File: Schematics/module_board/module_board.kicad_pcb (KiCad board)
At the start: 2 copper layers, 30 x 30 mm, 35 parts, among them J1 Conn_01x01_Male, J11 Conn_01x01_Male, J12 Conn_01x01_Male, J13 Conn_01x01_Male, J14 Conn_01x01_Male, J15 Conn_01x01_Male, J16 Conn_01x01_Male, J17 Conn_01x01_Male, J2 Conn_01x01_Male, J3 Conn_01x01_Male, J4 Conn_01x01_Male, J5 Conn_01x06_Male, U1 RP2040, U2 W25Q16JVSSIQ, Y1 ABLS-12.000MHZ-B4-T

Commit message: Module updates
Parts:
- removed J11, J12, J13, J14, J15, J16, J17: Conn_01x01_Male, Connector_Pin:Pin_D1.0mm_L10.0mm
- removed REF**, hello: MountingHole_3.2mm_M3, MountingHole:MountingHole_3.2mm_M3
- added J6: Conn_01x02_Female, Connector_PinHeader_2.54mm:PinHeader_1x02_P2.54mm_Vertical, F.Cu at (172.7, 77.3)
- added J7: Conn_01x02_Female, Connector_PinHeader_2.54mm:PinHeader_1x02_P2.54mm_Vertical, F.Cu at (172.0, 99.3)
- added J8: Conn_01x02_Female, Connector_PinHeader_2.54mm:PinHeader_1x02_P2.54mm_Vertical, F.Cu at (147.6, 86.4)
- added J9: Conn_01x02_Female, Connector_PinHeader_2.54mm:PinHeader_1x02_P2.54mm_Vertical, F.Cu at (147.6, 92.1)
- J5: footprint Prototroller:Mag_Pogo_6P_P2.2mm_Male -> prototroller_footprints:Mag_Pogo_6P_P2.2mm_Male
- Y1: footprint ABLS-12:XTAL_ABLS-12.000MHZ-B4-T -> prototroller_footprints:XTAL_ABLS-12.000MHZ-B4-T
- moved JP1 10.5 mm to (151.7, 88.2)
- moved C3 4.36 mm to (167.4, 81.6)
- moved C6 4.36 mm to (169.8, 81.6)
- moved C4 4.36 mm to (168.6, 81.6)
- moved C5 4.36 mm to (166.1, 81.6)
- moved R8 3.61 mm to (162.2, 77.4)
- moved U2 3.55 mm to (156.8, 80.5)
- moved C10 3.36 mm to (163.4, 77.4)
- moved C1 3.36 mm to (162.7, 80.1)
- moved J3 3.21 mm to (169.1, 96.3)
- moved Y1 2.62 mm to (158.4, 102.1)
- moved R5 2.13 mm to (151.0, 79.5)
- moved J2 2.05 mm to (165.5, 98.0)
- moved J4 2.05 mm to (163.3, 98.0)
- moved J1 2.05 mm to (167.7, 98.0)
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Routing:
- net +3V3: track 62.9 -> 75.5 mm, vias 4 -> 5
- net +1V1: track 17.8 -> 29.0 mm, vias 0 -> 4
- net /BOOTSEL_N: track 2.68 -> 10.0 mm
- net /QSPI_SD1: track 11.7 -> 15.6 mm
- net /GPIO27_ADC1: track 23.3 -> 20.3 mm, vias 2 -> 1
- net /QSPI_SD2: track 11.3 -> 8.42 mm, vias 2 -> 0
- net Net-(C8-Pad2): track 9.48 -> 6.87 mm
- net /QSPI_SCLK: track 5.72 -> 7.62 mm
- net /XTAL_IN: track 10.8 -> 12.7 mm
- net /QSPI_NSS: track 28.3 -> 26.5 mm
- net /QSPI_SD3: track 7.35 -> 8.84 mm
- net /SPI1_SCK: track 12.1 -> 10.8 mm, vias 0 -> 1
- net /RX: track 9.78 -> 10.9 mm
- net /GPIO26_ADC0: track 22.8 -> 21.9 mm, vias 2 -> 1
- net GND: track 17.5 -> 16.6 mm, vias 16 -> 15
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
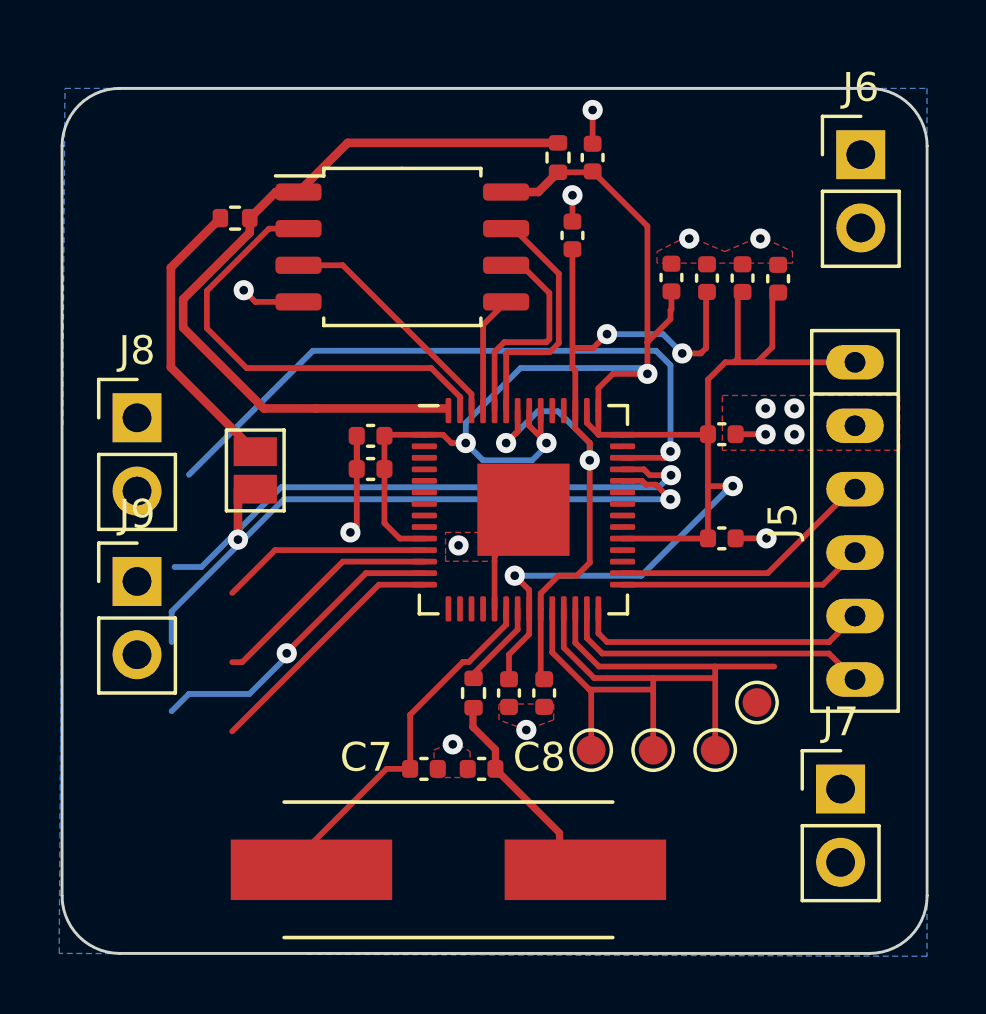
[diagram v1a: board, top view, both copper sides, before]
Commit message: Added 2.54mm pitch male headers for SPI1 pins and ADC pins
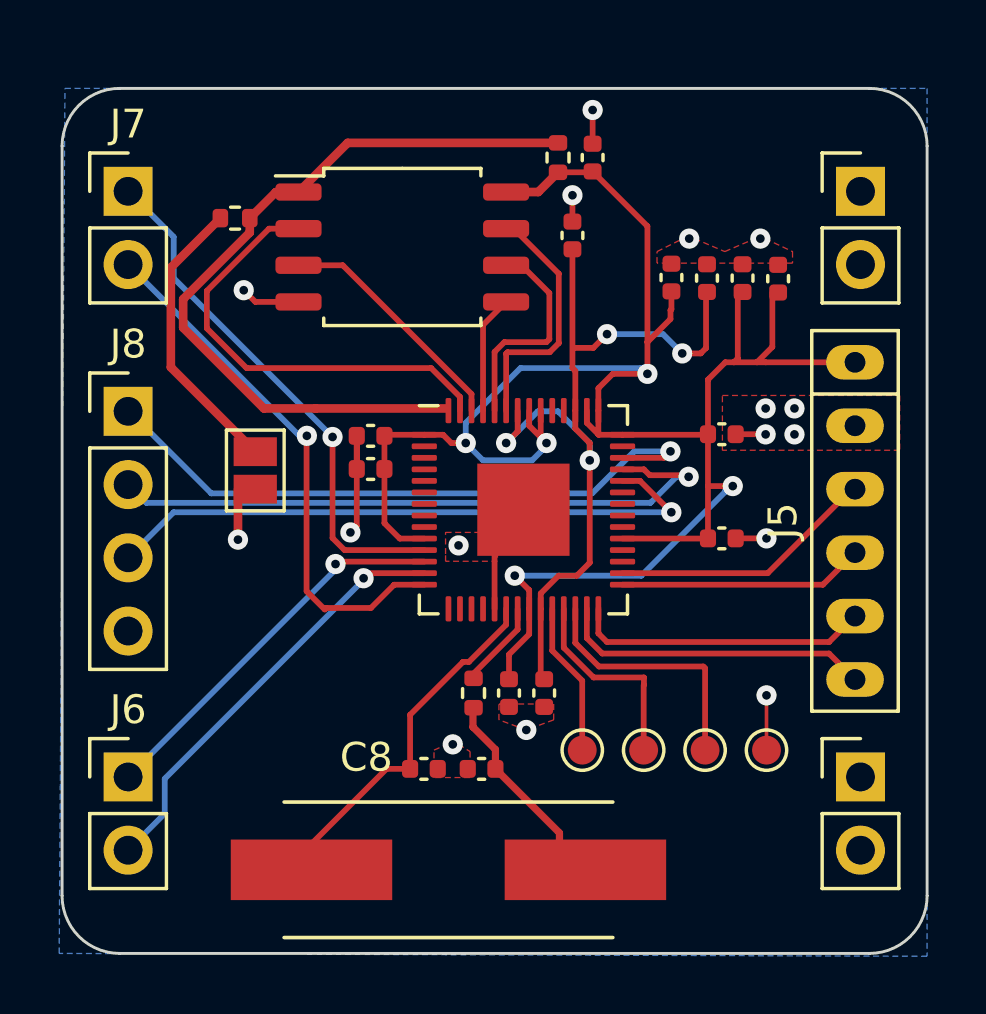
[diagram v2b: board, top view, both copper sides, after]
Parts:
- added J10: Conn_01x02_Male, Connector_PinHeader_2.54mm:PinHeader_1x02_P2.54mm_Vertical, F.Cu at (172.7, 78.6)
- J6, J7, J9: value Conn_01x02_Female -> Conn_01x02_Male
- J8: value Conn_01x02_Female -> Conn_01x04_Male; footprint Connector_PinHeader_2.54mm:PinHeader_1x02_P2.54mm_Vertical -> Connector_PinHeader_2.54mm:PinHeader_1x04_P2.54mm_Vertical
- moved J6 33.3 mm to (147.3, 98.9)
- moved J7 32.3 mm to (147.3, 78.6)
- moved J9 26.0 mm to (172.7, 98.9)
- moved J2 1.68 mm to (169.4, 98.0)
- moved J8 0.38 mm to (147.3, 86.2)
- moved J4 0.35 mm to (167.3, 98.0)
- moved J1 0.33 mm to (165.2, 98.0)
- moved J3 0.31 mm to (163.0, 98.0)
- renumbered C11 to C10, C12 to C11, C13 to C12, C14 to C13, C10 to C14, C9 to C7, C7 to C8, C8 to C9, J2 to J1, J3 to J2, J4 to J3, J1 to J4, R5 to R1, R8 to R2, R9 to R3
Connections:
- J6 pad 1: /GPIO28_ADC2 -> /SPI1_CS_IO9
- J6 pad 2: /GPIO27_ADC1 -> /SPI1_SCK
- J7 pad 1: /GPIO26_ADC0 -> /SPI1_RX
- J7 pad 2: unconnected-(J7-Pad2) -> /SPI1_TX
- J8 pad 1: /SPI1_CS_IO9 -> /GPIO28_ADC2
- J8 pad 2: /SPI1_SCK -> /GPIO27_ADC1
- J9 pad 1: /SPI1_RX -> unconnected-(J9-Pad1)
- J9 pad 2: /SPI1_TX -> unconnected-(J9-Pad2)
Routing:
- net /SPI1_RX: track 7.28 -> 18.3 mm, vias 0 -> 1
- net /SPI1_TX: track 8.77 -> 18.8 mm, vias 0 -> 1
- net /SPI1_CS_IO9: track 8.11 -> 13.5 mm, vias 0 -> 1
- net /SPI1_SCK: track 10.8 -> 15.0 mm
- net /RESET_N: track 11.3 -> 8.89 mm
- net /SWDIO: track 9.43 -> 7.07 mm
- net /SWCLK: track 7.55 -> 5.33 mm
- net /GPIO27_ADC1: track 20.3 -> 22.5 mm
- net GND: track 16.6 -> 18.5 mm, vias 15 -> 16
- net /GPIO28_ADC2: track 23.4 -> 22.3 mm

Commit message: Mod board finalizations
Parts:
- removed J2, J3, J4: Conn_01x01_Male, TestPoint:TestPoint_Pad_D1.0mm
- J1: value Conn_01x01_Male -> Conn_01x04_Male; footprint TestPoint:TestPoint_Pad_D1.0mm -> Connector_PinHeader_2.54mm:PinHeader_1x04_P2.54mm_Vertical
- moved C6 5.44 mm to (164.4, 81.8), turned to 0 degrees
- moved C1 4.47 mm to (160.7, 84.1), turned to 0 degrees
- moved J1 3.90 mm to (169.0, 97.2), turned to -90 degrees
- moved C13 3.68 mm to (167.1, 83.4), turned to 90 degrees
- moved C4 3.17 mm to (166.0, 83.4)
- moved C3 3.07 mm to (164.9, 83.4)
- moved C5 2.97 mm to (163.8, 83.4)
- moved C8 2.70 mm to (154.8, 98.7)
- moved C9 2.70 mm to (156.8, 98.7)
- moved R3 2.70 mm to (156.6, 96.1)
- moved C12 2.70 mm to (157.8, 96.1)
- moved C2 2.70 mm to (159.0, 96.1)
- moved C14 0.70 mm to (163.4, 78.1)
- moved R2 0.70 mm to (162.2, 78.1)
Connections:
- J1 pad 1: /SWDIO -> GND
- J8 pad 4: unconnected-(J8-Pad4) -> /GPIO25
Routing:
- net /GPIO25: track 0.00 -> 23.8 mm, vias 0 -> 1
- net +3V3: track 75.5 -> 85.7 mm, vias 5 -> 6
- net +1V1: track 29.0 -> 23.3 mm, vias 4 -> 2
- net /XTAL_OUT: track 3.04 -> 5.97 mm
- net Net-(C9-Pad2): track 6.87 -> 9.68 mm
- net /QSPI_SD1: track 15.6 -> 12.8 mm
- net /QSPI_SD3: track 8.84 -> 10.8 mm
- net /SWDIO: track 7.07 -> 5.17 mm
- net /QSPI_SD0: track 4.10 -> 5.80 mm
- net /QSPI_SCLK: track 7.62 -> 9.29 mm
- net /RESET_N: track 8.89 -> 7.33 mm
- net /GPIO28_ADC2: track 22.3 -> 20.9 mm
- net /BOOTSEL_N: track 10.0 -> 8.60 mm
- net /XTAL_IN: track 12.7 -> 13.8 mm
- net /QSPI_SD2: track 8.42 -> 9.42 mm
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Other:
- board text added: "25"
- board text added: "CK"
- board text added: "CS"
- board text added: "IO"
- board text added: "MOD BOARD REV A"
- board text added: "PROTOTROLLER"
- board text added: "R"
- board text added: "RX"
- board text added: "TX"

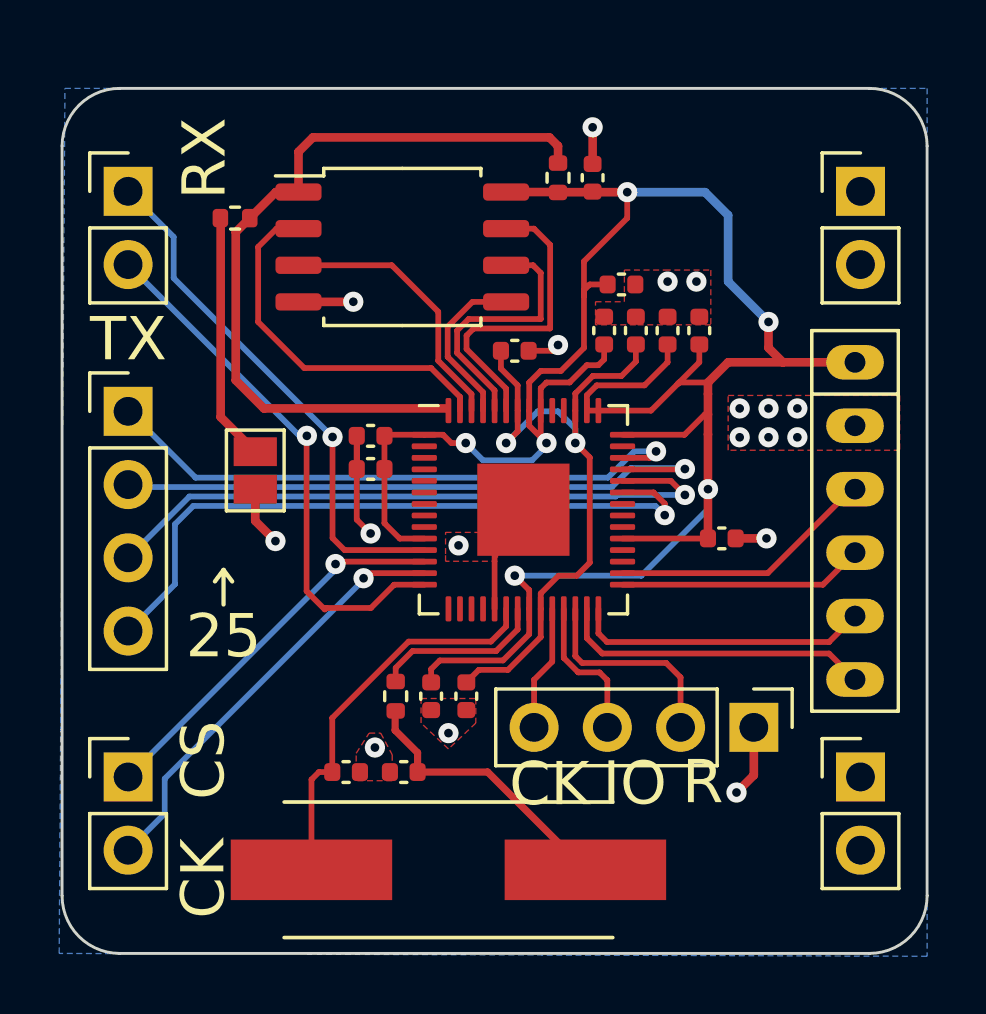
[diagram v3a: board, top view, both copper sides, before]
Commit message: improve clearance on module board edges
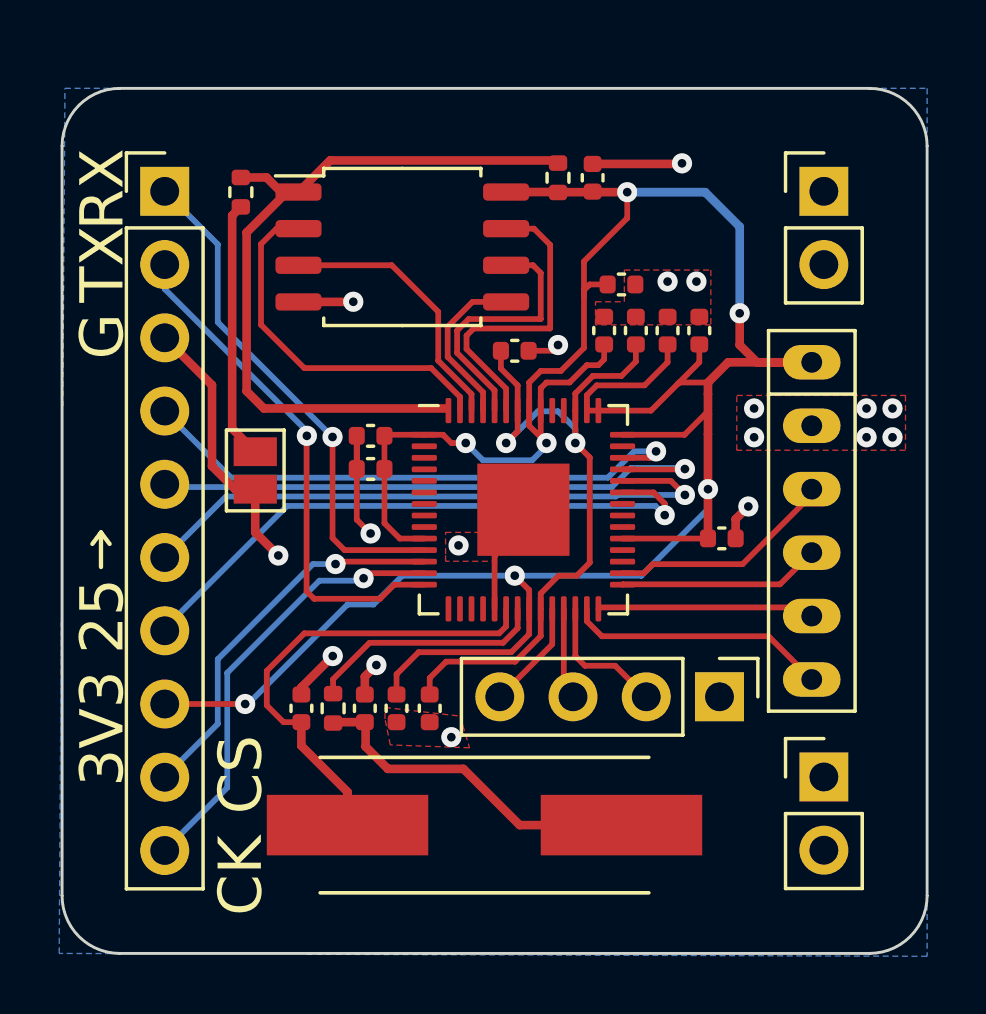
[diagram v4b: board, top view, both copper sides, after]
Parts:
- removed J6, J7: Conn_01x02_Male, Connector_PinHeader_2.54mm:PinHeader_1x02_P2.54mm_Vertical
- removed J8: Conn_01x04_Male, Connector_PinHeader_2.54mm:PinHeader_1x04_P2.54mm_Vertical
- added J2: Conn_01x10_Male, Connector_PinHeader_2.54mm:PinHeader_1x10_P2.54mm_Vertical, F.Cu at (148.6, 78.6)
- moved C8 2.70 mm to (153.3, 96.5), turned to -90 degrees
- moved C9 2.59 mm to (155.5, 96.5), turned to -90 degrees
- moved R3 2.21 mm to (154.4, 96.5)
- moved Y1 1.99 mm to (159.7, 100.5)
- moved J1 1.59 mm to (167.8, 96.1)
- moved J5 1.50 mm to (171.0, 90.0)
- moved C2 1.34 mm to (157.8, 96.5)
- moved C12 1.27 mm to (156.6, 96.5)
- moved J10 1.27 mm to (171.4, 78.6)
- moved J9 1.27 mm to (171.4, 98.9)
- moved R1 0.92 mm to (151.2, 78.6), turned to 90 degrees
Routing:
- net +3V3: track 85.7 -> 100.3 mm, vias 6 -> 7
- net GND: track 18.5 -> 28.5 mm
- net /CS: track 10.2 -> 7.54 mm
- net /RESET_N: track 7.33 -> 4.68 mm
- net /XTAL_IN: track 13.8 -> 16.4 mm
- net /GPIO25: track 23.8 -> 21.3 mm
- net /XTAL_OUT: track 5.97 -> 8.30 mm
- net Net-(C9-Pad2): track 9.68 -> 12.0 mm
- net /SWDIO: track 5.17 -> 3.18 mm
- net /RX: track 10.9 -> 9.07 mm
- net +1V1: track 23.3 -> 25.1 mm
- net /SCLK: track 8.52 -> 7.02 mm
- net /TX: track 9.27 -> 7.89 mm
- net /GPIO28_ADC2: track 20.9 -> 19.6 mm
- net /GPIO26_ADC0: track 22.6 -> 21.3 mm
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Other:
- board text added: "3V3"
- board text added: "G"
- board text added: "GN"
- board text added: "RES"
- board text removed: "R"

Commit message: Final improvements
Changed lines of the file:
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@@
       (pts
         (xy 159.130238 97.868975)
-        (xy 156.381832 97.768975)
-        (xy 156.2 96.869635)
-        (xy 156.2 96.469635)
-        (xy 158.8 96.769635)
+        (xy 156.05 97.67)
+        (xy 155.98 96.81)
+        (xy 156 96.34)
+        (xy 158.77 96.49)
       )
     )
